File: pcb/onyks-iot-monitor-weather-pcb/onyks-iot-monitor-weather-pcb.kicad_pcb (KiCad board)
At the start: 2 copper layers, 100 x 82 mm, 32 parts, among them J1 53398-0371, J10 Conn_01x02_Pin, J11 Conn_01x06_Pin, J12 Conn_02x05_Odd_Even, J13 Conn_01x02_Pin, J2 53398-0371, J3 53048-0810, J4 53398-0371, J5 53398-0371, J6 53398-0371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

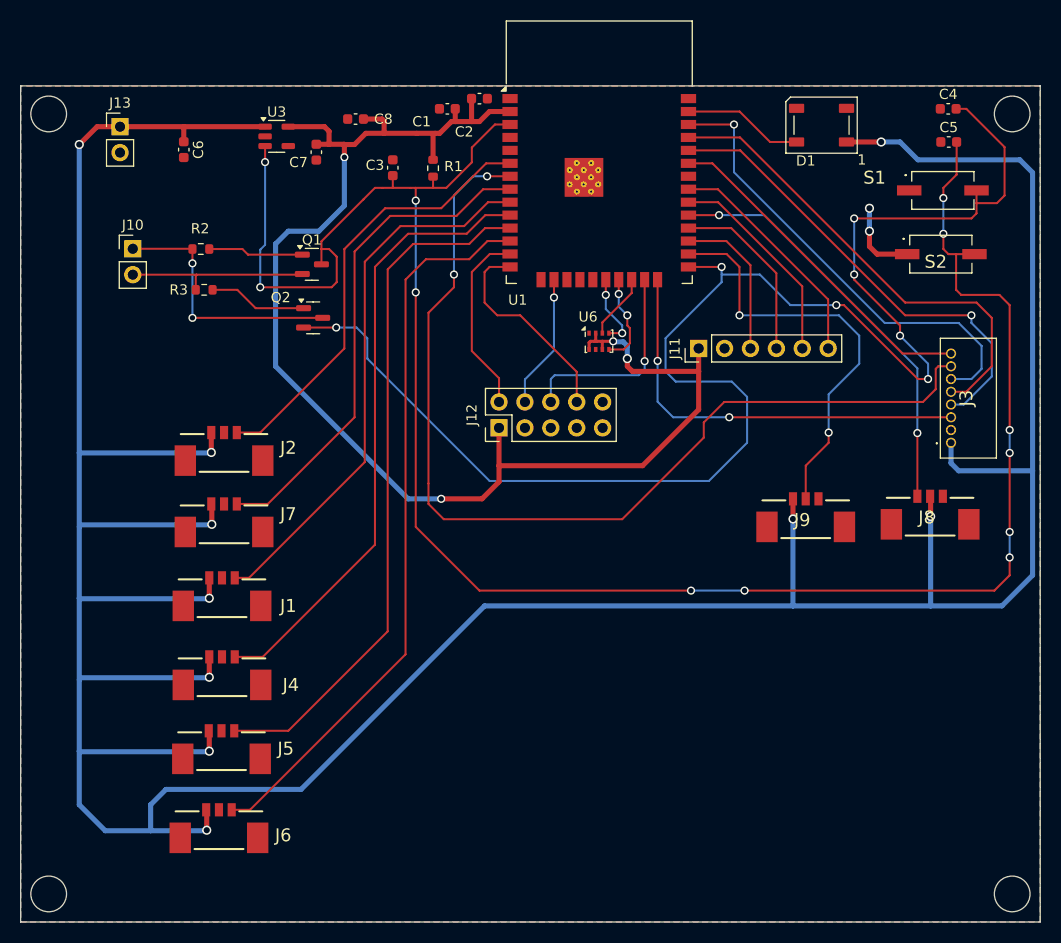
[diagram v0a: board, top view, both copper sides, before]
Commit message: Design Rules - Thermal relief problem partially solved
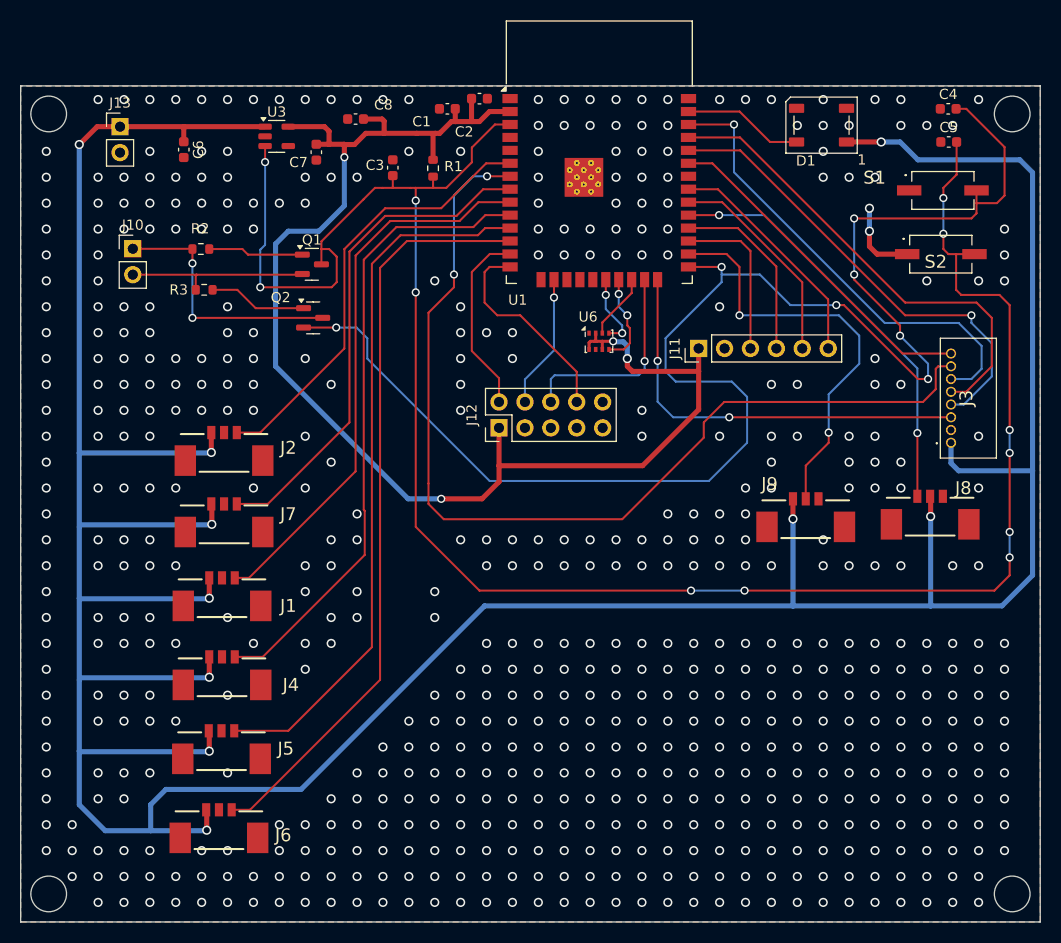
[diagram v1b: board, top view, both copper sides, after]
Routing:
- net /Hall 3: track 71.9 -> 74.1 mm
- net /Hall 2: track 68.3 -> 69.5 mm
- net /Hall 1: track 60.9 -> 62.0 mm
- net /Hall 6: track 53.8 -> 54.7 mm
- net /UART_PROGRAM_RXD: track 15.2 -> 16.0 mm
- net GND: vias 2 -> 592
